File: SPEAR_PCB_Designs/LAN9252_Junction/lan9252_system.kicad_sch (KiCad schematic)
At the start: 30 parts, among them J8 Conn_01x02_Pin, U1 LAN9252_ML, Y1 25MHz

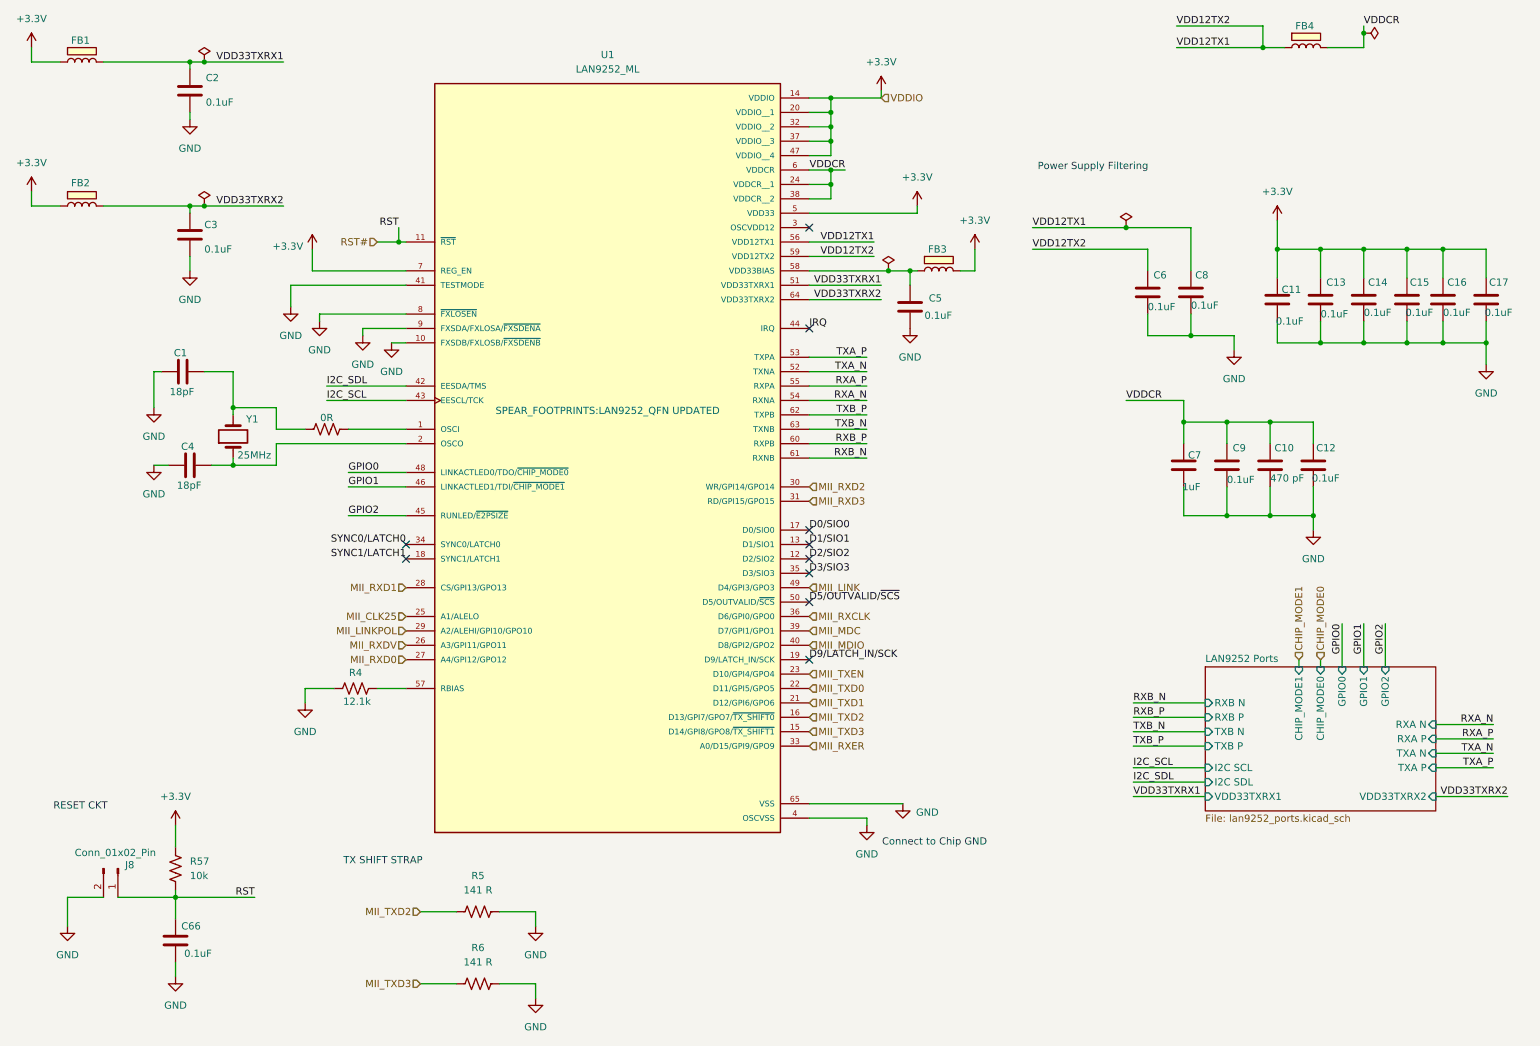
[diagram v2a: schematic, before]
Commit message: Added Fabrication Spec
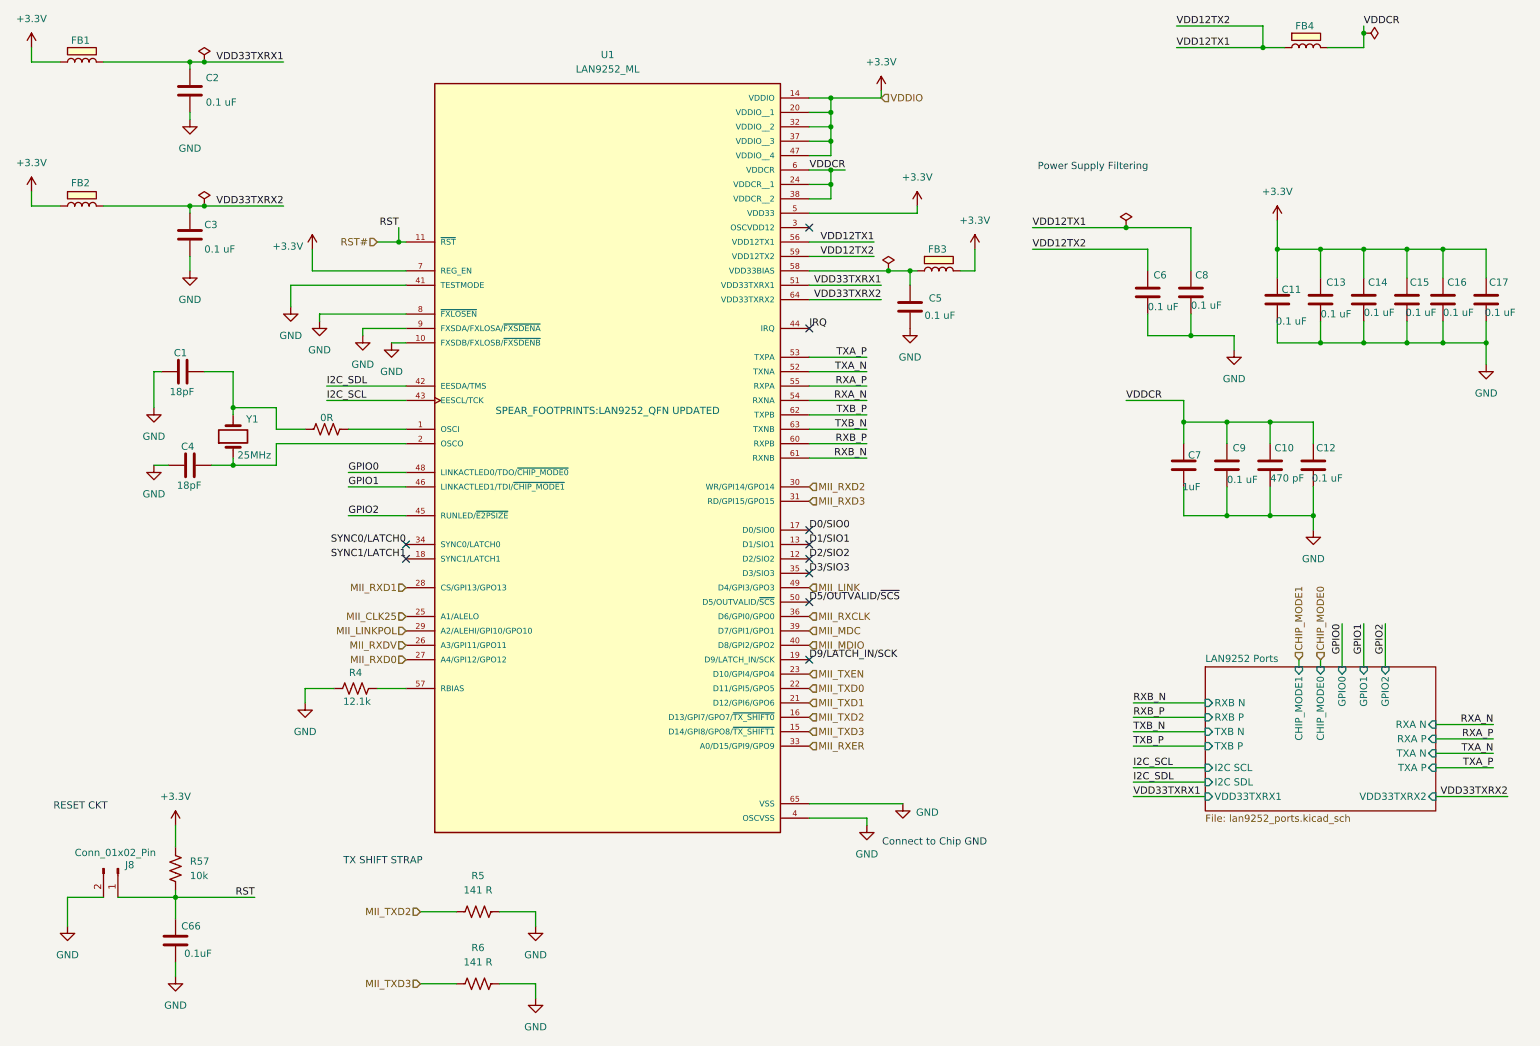
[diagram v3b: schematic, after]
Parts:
- C1, C4: DigiKey_Part_Number (none) -> 1276-6612-1-ND
- C10: DigiKey_Part_Number (none) -> 1276-1566-1-ND
- C11, C12, C13, C14, C15, C16, C17, C2, C3, C5, C6, C8, C9: value 0.1uF -> 0.1 uF; DigiKey_Part_Number (none) -> 445-5932-1-ND
- C7: DigiKey_Part_Number (none) -> 4713-GMC04X5R105K50NTTR-ND
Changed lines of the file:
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@@
 			)
 		)
-		(property "Value" "0.1uF"
+		(property "Value" "0.1 uF"
 			(at 238.506 69.85 0)
 			(effects
@@
 			)
 		)
+		(property "DigiKey_Part_Number" "445-5932-1-ND"
+			(at 238.76 66.04 0)
+			(effects
+				(font
+					(size 1.27 1.27)
+				)
+				(hide yes)
+			)
+		)
 		(pin "2"
 		)
@@
 			)
 		)
-		(property "Value" "0.1uF"
+		(property "Value" "0.1 uF"
 			(at 246.38 68.58 0)
 			(effects
@@
 			)
 		)
+		(property "DigiKey_Part_Number" "445-5932-1-ND"
+			(at 246.38 66.04 0)
+			(effects
+				(font
+					(size 1.27 1.27)
+				)
+				(hide yes)
+			)
+		)
 		(pin "2"
 		)
@@
 			)
 		)
-		(property "Value" "0.1uF"
+		(property "Value" "0.1 uF"
 			(at 215.9 67.31 0)
 			(effects
@@
 			)
 		)
+		(property "DigiKey_Part_Number" "445-5932-1-ND"
+			(at 215.9 64.77 0)
+			(effects
+				(font
+					(size 1.27 1.27)
+				)
+				(hide yes)
+			)
+		)
 		(pin "2"
 		)
@@
 			)
 		)
+		(property "DigiKey_Part_Number" "4713-GMC04X5R105K50NTTR-ND"
+			(at 222.25 95.25 0)
+			(effects
+				(font
+					(size 1.27 1.27)
+				)
+				(hide yes)
+			)
+		)
 		(pin "2"
 		)
@@
 			)
 		)
-		(property "Value" "0.1uF"
+		(property "Value" "0.1 uF"
 			(at 49.53 57.15 0)
 			(effects
@@
 			)
 		)
+		(property "DigiKey_Part_Number" "445-5932-1-ND"
+			(at 46.99 54.61 0)
+			(effects
+				(font
+					(size 1.27 1.27)
+				)
+				(hide yes)
+			)
+		)
 		(pin "2"
 		)
@@
 			)
 		)
-		(property "Value" "0.1uF"
+		(property "Value" "0.1 uF"
 			(at 254 68.326 0)
 			(effects
@@
 			)
 		)
+		(property "DigiKey_Part_Number" "445-5932-1-ND"
+			(at 254 66.04 0)
+			(effects
+				(font
+					(size 1.27 1.27)
+				)
+				(hide yes)
+			)
+		)
 		(pin "2"
 		)
@@
 			)
 		)
-		(property "Value" "0.1uF"
+		(property "Value" "0.1 uF"
 			(at 244.856 97.536 0)
 			(effects
@@
 			)
 		)
+		(property "DigiKey_Part_Number" "445-5932-1-ND"
+			(at 245.11 95.25 0)
+			(effects
+				(font
+					(size 1.27 1.27)
+				)
+				(hide yes)
+			)
+		)
 		(pin "2"
 		)
@@
 			)
 		)
+		(property "DigiKey_Part_Number" "1276-1566-1-ND"
+			(at 237.49 95.25 0)
+			(effects
+				(font
+					(size 1.27 1.27)
+				)
+				(hide yes)
+			)
+		)
 		(pin "2"
 		)
@@
 			)
 		)
-		(property "Value" "0.1uF"
+		(property "Value" "0.1 uF"
 			(at 275.336 68.326 0)
 			(effects
@@
 			)
 		)
+		(property "DigiKey_Part_Number" "445-5932-1-ND"
+			(at 275.59 66.04 0)
+			(effects
+				(font
+					(size 1.27 1.27)
+				)
+				(hide yes)
+			)
+		)
 		(pin "2"
 		)
@@
 			)
 		)
-		(property "Value" "0.1uF"
+		(property "Value" "0.1 uF"
 			(at 261.366 68.326 0)
 			(effects
@@
 			)
 		)
+		(property "DigiKey_Part_Number" "445-5932-1-ND"
+			(at 261.62 66.04 0)
+			(effects
+				(font
+					(size 1.27 1.27)
+				)
+				(hide yes)
+			)
+		)
 		(pin "2"
 		)
@@
 			)
 		)
-		(property "Value" "0.1uF"
+		(property "Value" "0.1 uF"
 			(at 176.53 68.834 0)
 			(effects
@@
 			)
 		)
+		(property "DigiKey_Part_Number" "445-5932-1-ND"
+			(at 173.99 67.31 0)
+			(effects
+				(font
+					(size 1.27 1.27)
+				)
+				(hide yes)
+			)
+		)
 		(pin "2"
 		)
@@
 			)
 		)
+		(property "DigiKey_Part_Number" "1276-6612-1-ND"
+			(at 45.72 78.74 90)
+			(effects
+				(font
+					(size 1.27 1.27)
+				)
+				(hide yes)
+			)
+		)
 		(pin "1"
 		)
@@
 			)
 		)
-		(property "Value" "0.1uF"
+		(property "Value" "0.1 uF"
 			(at 229.87 97.79 0)
 			(effects
@@
 			)
 		)
+		(property "DigiKey_Part_Number" "445-5932-1-ND"
+			(at 229.87 95.25 0)
+			(effects
+				(font
+					(size 1.27 1.27)
+				)
+				(hide yes)
+			)
+		)
 		(pin "2"
 		)
@@
 			)
 		)
-		(property "Value" "0.1uF"
+		(property "Value" "0.1 uF"
 			(at 49.784 31.242 0)
 			(effects
@@
 			)
 		)
+		(property "DigiKey_Part_Number" "445-5932-1-ND"
+			(at 46.99 29.21 0)
+			(effects
+				(font
+					(size 1.27 1.27)
+				)
+				(hide yes)
+			)
+		)
 		(pin "2"
 		)
@@
 			)
 		)
-		(property "Value" "0.1uF"
+		(property "Value" "0.1 uF"
 			(at 267.97 68.326 0)
 			(effects
@@
 			)
 		)
+		(property "DigiKey_Part_Number" "445-5932-1-ND"
+			(at 267.97 66.04 0)
+			(effects
+				(font
+					(size 1.27 1.27)
+				)
+				(hide yes)
+			)
+		)
 		(pin "2"
 		)
@@
 			)
 		)
+		(property "DigiKey_Part_Number" "1276-6612-1-ND"
+			(at 46.99 95.25 90)
+			(effects
+				(font
+					(size 1.27 1.27)
+				)
+				(hide yes)
+			)
+		)
 		(pin "1"
 		)
@@
 			)
 		)
-		(property "Value" "0.1uF"
+		(property "Value" "0.1 uF"
 			(at 223.52 67.056 0)
 			(effects
@@
 			(at 223.52 64.77 0)
 			(effects
+				(font
+					(size 1.27 1.27)
+				)
+				(hide yes)
+			)
+		)
+		(property "DigiKey_Part_Number" "445-5932-1-ND"
+			(at 223.52 64.77 0)
+			(effects

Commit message: Added BOM for the Junction Board
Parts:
- C66: DigiKey_Part_Number (none) -> 4713-GMC02X5R104K35NTCT-ND
- FB1, FB3, FB4: DigiKey_Part_Number (none) -> 490-3992-1-ND
- FB2: value FerriteBead -> BLM18EG221SN1D; DigiKey_Part_Number (none) -> 490-3992-1-ND
- J8: DigiKey_Part_Number (none) -> 2057-PH1-02-UA-ND
- R3: DigiKey_Part_Number (none) -> 311-0.0JRCT-ND
- R4: DigiKey_Part_Number (none) -> 311-12.1KLRCT-ND
- R5, R6: DigiKey_Part_Number (none) -> 2019-RN73R1ETTP1420B50CT-ND
- R57: DigiKey_Part_Number (none) -> 311-10KJRCT-ND
- U1: DigiKey_Part_Number (none) -> LAN9252I/ML-ND
- Y1: DigiKey_Part_Number (none) -> 732-830056463CT-ND
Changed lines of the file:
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@@
 			)
 		)
+		(property "DigiKey_Part_Number" "490-3992-1-ND"
+			(at 176.53 60.96 0)
+			(effects
+				(font
+					(size 1.27 1.27)
+				)
+				(hide yes)
+			)
+		)
 		(pin "1"
 		)
@@
 			)
 		)
+		(property "DigiKey_Part_Number" "490-3992-1-ND"
+			(at 25.4 24.13 0)
+			(effects
+				(font
+					(size 1.27 1.27)
+				)
+				(hide yes)
+			)
+		)
 		(pin "1"
 		)
@@
 			)
 		)
+		(property "DigiKey_Part_Number" "4713-GMC02X5R104K35NTCT-ND"
+			(at 44.45 179.07 0)
+			(effects
+				(font
+					(size 1.27 1.27)
+				)
+				(hide yes)
+			)
+		)
 		(pin "1"
 		)
@@
 			)
 		)
+		(property "DigiKey_Part_Number" "732-830056463CT-ND"
+			(at 54.61 90.17 90)
+			(effects
+				(font
+					(size 1.27 1.27)
+				)
+				(hide yes)
+			)
+		)
 		(pin "1"
 		)
@@
 			)
 		)
+		(property "DigiKey_Part_Number" "311-0.0JRCT-ND"
+			(at 71.12 88.9 90)
+			(effects
+				(font
+					(size 1.27 1.27)
+				)
+				(hide yes)
+			)
+		)
 		(pin "1"
 		)
@@
 			)
 		)
+		(property "DigiKey_Part_Number" "311-10KJRCT-ND"
+			(at 44.45 166.37 0)
+			(effects
+				(font
+					(size 1.27 1.27)
+				)
+				(hide yes)
+			)
+		)
 		(pin "1"
 		)
@@
 			)
 		)
+		(property "DigiKey_Part_Number" "2019-RN73R1ETTP1420B50CT-ND"
+			(at 97.79 173.99 90)
+			(effects
+				(font
+					(size 1.27 1.27)
+				)
+				(hide yes)
+			)
+		)
 		(pin "1"
 		)
@@
 			)
 		)
+		(property "DigiKey_Part_Number" "LAN9252I/ML-ND"
+			(at 120.65 86.36 0)
+			(effects
+				(font
+					(size 1.27 1.27)
+				)
+				(hide yes)
+			)
+		)
 		(pin "34"
 		)
@@
 			)
 		)
+		(property "DigiKey_Part_Number" "2057-PH1-02-UA-ND"
+			(at 34.29 166.37 90)
+			(effects
+				(font
+					(size 1.27 1.27)
+				)
+				(hide yes)
+			)
+		)
 		(pin "1"
 		)
@@
 			)
 		)
+		(property "DigiKey_Part_Number" "490-3992-1-ND"
+			(at 241.3 21.59 0)
+			(effects
+				(font
+					(size 1.27 1.27)
+				)
+				(hide yes)
+			)
+		)
 		(pin "1"
 		)
@@
 			)
 		)
+		(property "DigiKey_Part_Number" "311-12.1KLRCT-ND"
+			(at 76.2 134.62 90)
+			(effects
+				(font
+					(size 1.27 1.27)
+				)
+				(hide yes)
+			)
+		)
 		(pin "1"
 		)
@@
 			)
 		)
+		(property "DigiKey_Part_Number" "2019-RN73R1ETTP1420B50CT-ND"
+			(at 97.79 186.69 90)
+			(effects
+				(font
+					(size 1.27 1.27)
+				)
+				(hide yes)
+			)
+		)
 		(pin "1"
 		)
@@
 			)
 		)
-		(property "Value" "FerriteBead"
+		(property "Value" "BLM18EG221SN1D"
 			(at 27.432 51.562 0)
 			(effects
@@
 			)
 		)
+		(property "DigiKey_Part_Number" "490-3992-1-ND"
+			(at 25.4 49.53 0)
+			(effects
+				(font
+					(size 1.27 1.27)
+				)
+				(hide yes)
+			)
+		)
 		(pin "1"
 		)
@@
 				)
 				(path "/16d72164-3a84-4f74-a868-383d0ad57128/52e6a653-4436-4d7a-ae83-cfeea5b0a028"
-					(reference "FB6")
+					(reference "FB2")
 					(unit 1)
 				)
